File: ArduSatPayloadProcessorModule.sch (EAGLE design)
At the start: 315 parts, among them IC1 ATMEGA328P QFN32, IC10 ATMEGA328P QFN32, IC11 ATMEGA328P QFN32, IC12 ATMEGA328P QFN32, IC13 ATMEGA328P QFN32, IC14 ATMEGA328P QFN32, IC15 ATMEGA328P QFN32, IC16 ATMEGA328P QFN32, IC17 TXB0104, IC18 TMP102, IC19 TMP102, IC2 ATMEGA328P QFN32, IC20 ATMEGA2561-16MU, IC21 MAX4372F, IC22 MAX4372F, IC23 MUX-74HC4067-QFNSMT, IC24 MUX-74HC4067-QFNSMT, IC3 ATMEGA328P QFN32, IC4 ATMEGA328P QFN32, IC5 ATMEGA328P QFN32, IC6 ATMEGA328P QFN32, IC7 ATMEGA328P QFN32, IC8 ATMEGA328P QFN32, IC9 ATMEGA328P QFN32, P1 microSD, Q1 RJU003N03 N-MOSFET, Q10 RJU003N03 N-MOSFET, Q11 RJU003N03 N-MOSFET, Q12 RJU003N03 N-MOSFET, Q13 RJU003N03 N-MOSFET, Q14 RJU003N03 N-MOSFET, Q15 RJU003N03 N-MOSFET, Q16 RJU003N03 N-MOSFET, Q17 RJU003N03 N-MOSFET, Q18 RJU003N03 N-MOSFET, Q19 RJU003N03 N-MOSFET, Q2 RJU003N03 N-MOSFET, Q20 RJU003N03 N-MOSFET, Q21 RJU003N03 N-MOSFET, Q22 RJU003N03 N-MOSFET, Q23 RJU003N03 N-MOSFET, Q24 RJU003N03 N-MOSFET, Q25 RJU003N03 N-MOSFET, Q26 RJU003N03 N-MOSFET, Q27 RJU003N03 N-MOSFET, Q28 RJU003N03 N-MOSFET, Q29 RJU003N03 N-MOSFET, Q3 RJU003N03 N-MOSFET, Q30 RJU003N03 N-MOSFET, Q31 RJU003N03 N-MOSFET, Q32 RJU003N03 N-MOSFET, Q33 RJU003N03 N-MOSFET, Q34 RJU003N03 N-MOSFET, Q35 RJU003N03 N-MOSFET, Q36 RJU003N03 N-MOSFET, Q39 RJU003N03 N-MOSFET, Q4 RJU003N03 N-MOSFET, Q40 RJU003N03 N-MOSFET, Q41 RJU003N03 N-MOSFET, Q42 RJU003N03 N-MOSFET, Q43 RJU003N03 N-MOSFET, Q44 RJU003N03 N-MOSFET, Q45 RJU003N03 N-MOSFET, Q46 RJU003N03 N-MOSFET, Q5 RJU003N03 N-MOSFET, Q6 RJU003N03 N-MOSFET, Q7 RJU003N03 N-MOSFET, Q8 RJU003N03 N-MOSFET, Q9 RJU003N03 N-MOSFET, SW1 ADG801 SOT23-6, SW10 ADG801 SOT23-6, SW11 ADG801 SOT23-6, SW12 ADG801 SOT23-6, SW13 ADG801 SOT23-6, SW14 ADG801 SOT23-6, SW15 ADG801 SOT23-6, SW16 ADG801 SOT23-6, SW17 RESET, SW2 ADG801 SOT23-6, SW3 ADG801 SOT23-6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

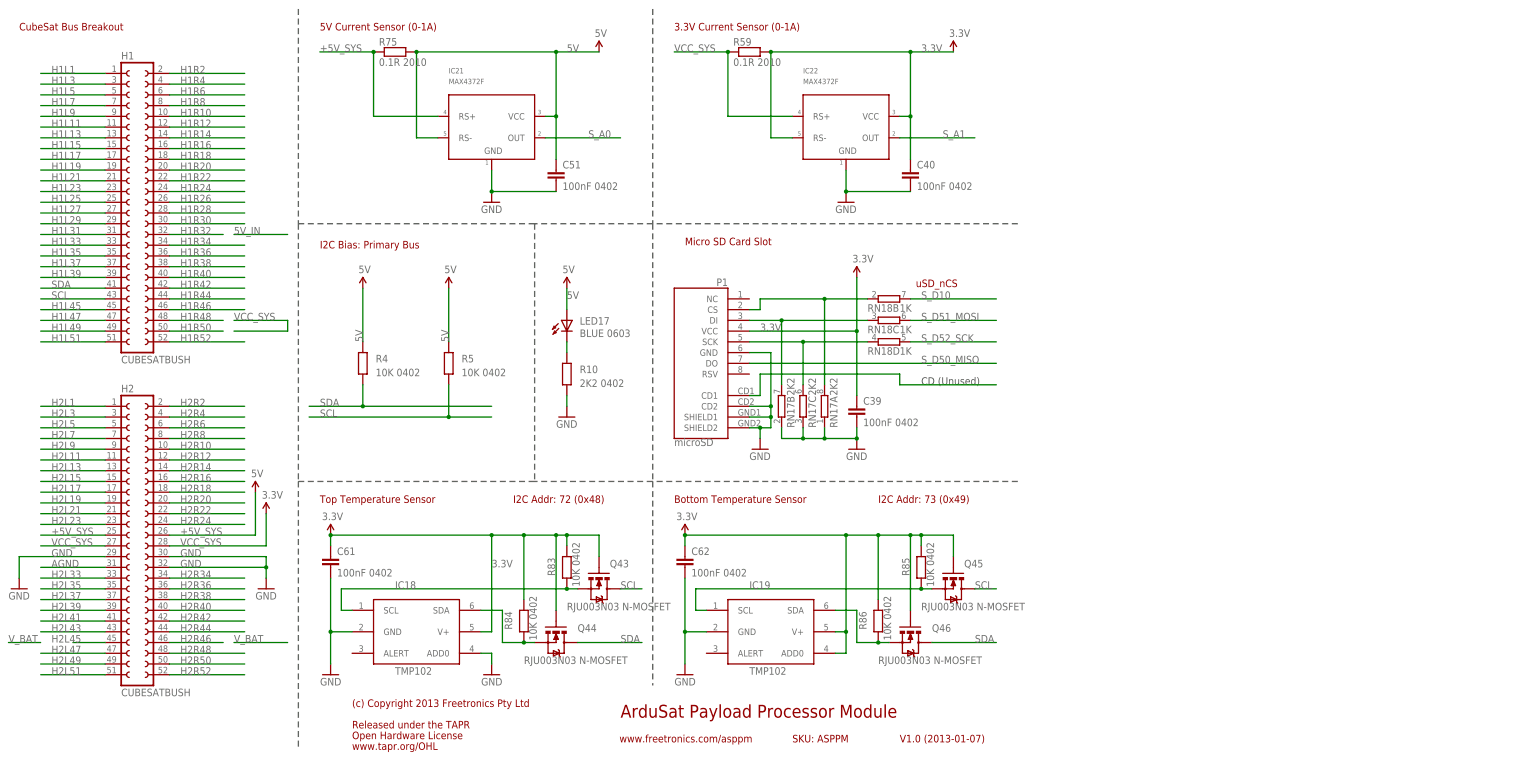
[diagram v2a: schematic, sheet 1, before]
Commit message: Fixed ISP pin assignment Added D13 LED to supervisor Fixed TX/RX from supervisor to multiplexers Replaced 4-pin debug connector with 6-pin connector in FTDI-type format Linked supervisor reset to debug connector GPS power now controlled by supervisor Input power from debug connector now goes through 5V current sensor Switched Cubesat Bus power links to H1-51 (5V) and H1-52 (3.3V) Added cut-track jumpers to select power link source Linked debug console to Cubesat Bus H1-34 (TXO) and H1-36 (RXD) Moved debug connector away from edge to increase solar panel clearance
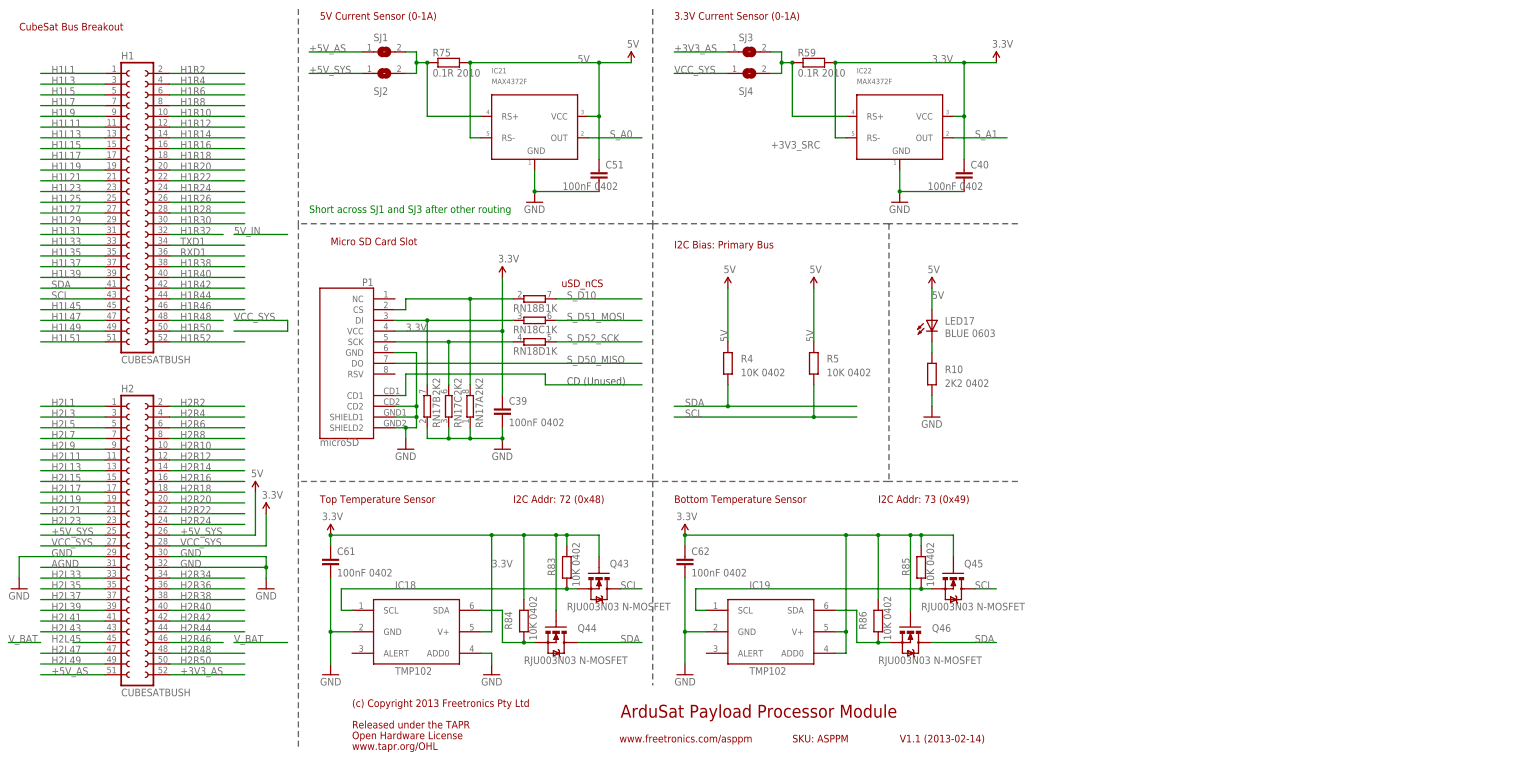
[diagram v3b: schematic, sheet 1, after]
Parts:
- added C58: 100nF 0402, freetronics-jon:C-EU0402C
- added LED18: BLUE 0603, freetronics-jon:LED0402
- added R81: 2K2 0402, freetronics-jon:RESISTOR0402
- added SJ1, SJ2, SJ3, SJ4: (no value), freetronics-master-v1.1:SJ
- added SW18: ADG801 SOT23-6, freetronics-jon:ADG801SOT23-6
- C13, C14: value 22pF 0603 -> 22pF 0402
- JP1: device pinhead:PINHD-1X4/90 -> freetronics-master-v1:M06RA
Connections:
- removed net AREF: C14.2, IC20.XTAL1, R32.1, XTL17.XTL2
- removed net H1R34: H1.34
- removed net H1R36: H1.36
- removed net H2L51: H2.51
- removed net H2R52: H2.52
- new net +3V3_AS: H2.52, SJ3.1
- new net +3V3_SRC: IC22.RS+, R59.1, SJ3.2, SJ4.2
- new net +5V_AS: H2.51, SJ1.1
- new net +5V_SRC: IC21.RS+, JP1.3, R75.1, SJ1.2, SJ2.2
- new net GPS_5V: C60.+, SW18.D, X2-1.S
- new net N$9998: LED18.C, R81.2
- new net PWR_GPS: IC20.(T1)PD6, SW18.IN
- new net RTS: C58.1, JP1.6
- new net XTAL2: C13.2, IC20.XTAL2, R32.2, XTL17.XTL1
- net +5V_SYS: now also SJ2.1; no longer IC21.RS+, R75.1
- net 5V: now also SW18.S, SW18.VDD; no longer C60.+, JP1.2, X2-1.S
- net D0_RX: now also H19.4, IC23.Z; no longer IC24.Z
- net D1_TX: now also H19.1, IC24.Z; no longer IC23.Z
- net GND: now also JP1.2, R81.1, SW18.GND
- net RXD1: now also H1.36, JP1.4; no longer JP1.3
- net S_D13: now also LED18.A
- net S_D50_MISO: no longer H19.1
- net S_D51_MOSI: no longer H19.4
- net S_RESET: now also C58.2
- net TXD1: now also H1.34, JP1.5; no longer JP1.4
- net VCC_SYS: now also SJ4.1; no longer IC22.RS+, R59.1
- net XTAL1: now also C14.2, IC20.XTAL1, R32.1, XTL17.XTL2; no longer C13.2, IC20.XTAL2, R32.2, XTL17.XTL1
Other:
- note added: "GPS Power Control"
- note added: "Short across SJ1 and SJ3 after other routing"
- note added: "TODO: DONE: Add D13 LED to supervisor Fix TX/RX to multiplexors Fix supervisor PDI / PDO Make debug console match FTDI standard Control GPS power from supervisor Monitor current when powered via console port Power from different bus pins. SJs to existing pins. Route 5V from H1-51 instead of H2-25/26 Route 3.3V from H1-52 instead of H2-27/28 Lay out debug USART1 to stack header on positions H1-34 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"
- note added: "V1.1 (2013-02-14)"
- note removed: "Debug was connected to VCC_SYS, I switched it to 5V. Is that OK?"
- note removed: "V1.0 (2013-01-07)"
- moved on the sheet: C39, C40, C51, IC21, IC22, LED17, P1, R10, R4, R5, R59, R75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

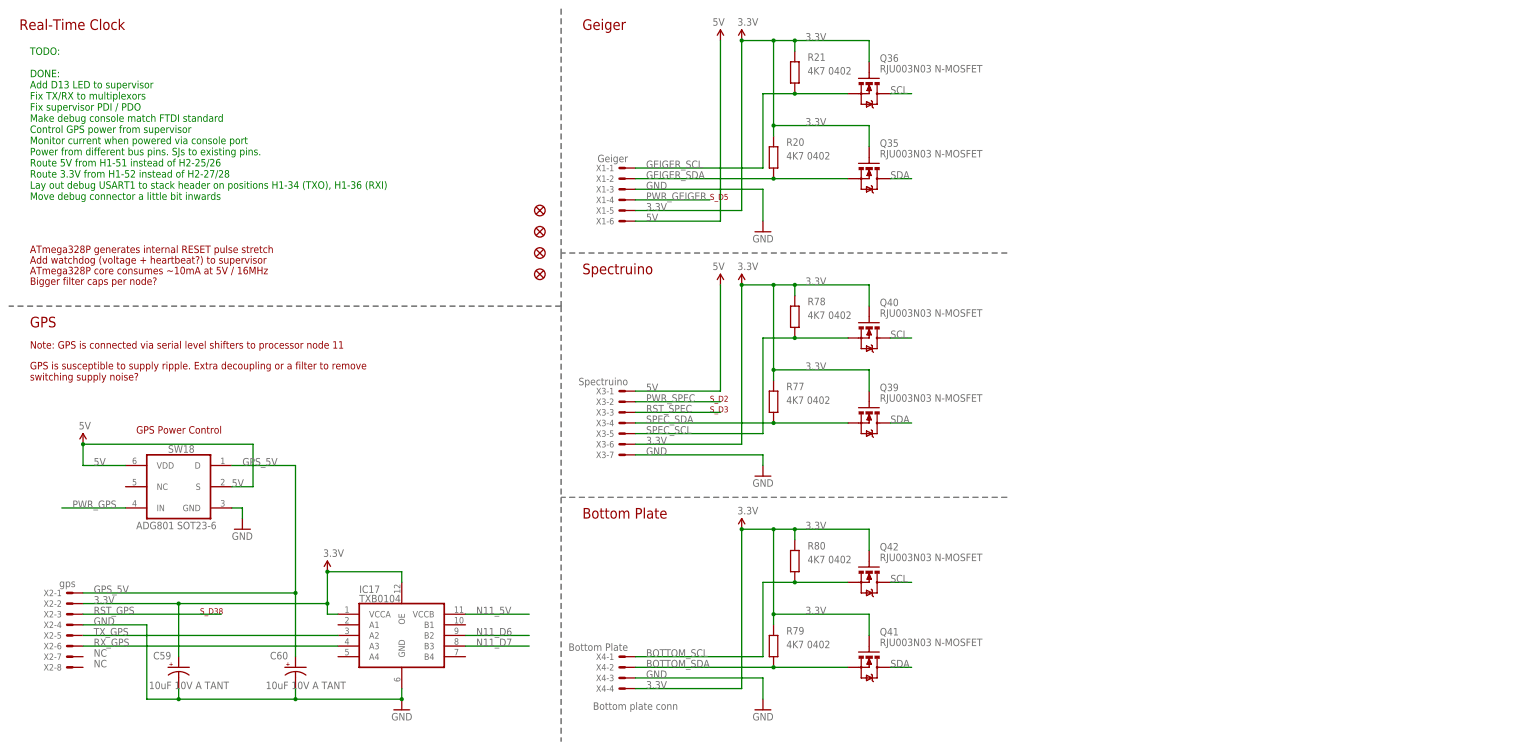
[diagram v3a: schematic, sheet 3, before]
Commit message: Added labels for power source selection jumpers; added parts for node reset latch
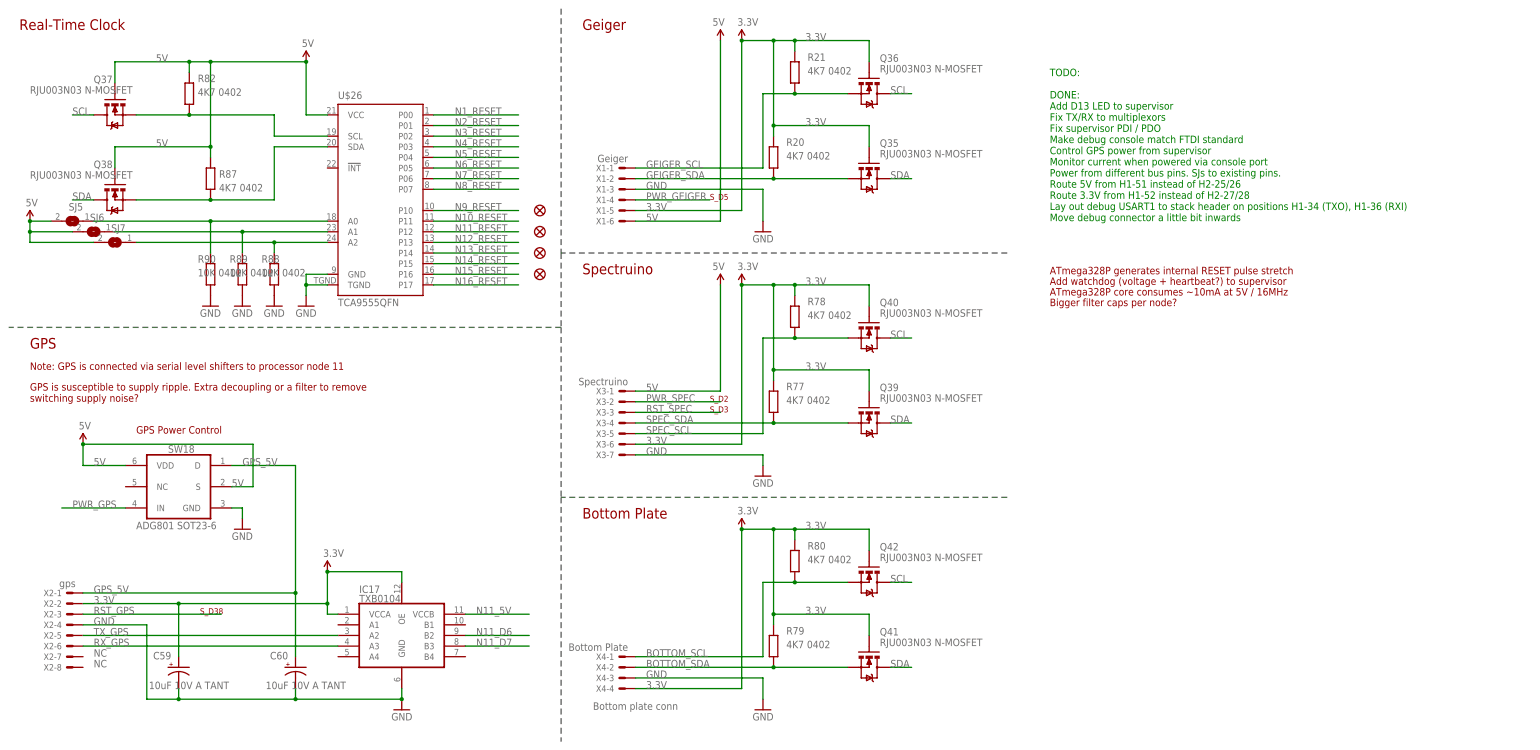
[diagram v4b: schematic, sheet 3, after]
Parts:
- added Q37, Q38: RJU003N03 N-MOSFET, freetronics-jon:MOSFET-NSOT-323
- added R82, R87: 4K7 0402, freetronics-jon:RESISTOR0402
- added R88, R89, R90: 10K 0402, freetronics-jon:RESISTOR0402
- added SJ5, SJ6, SJ7: (no value), freetronics-master-v1:SJ
- added U$26: TCA9555QFN, freetronics-jon:TCA9555QFN
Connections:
- removed net H1L51: H1.51
- removed net H1R52: H1.52
- new net H2L51: H2.51
- new net H2R52: H2.52
- new net N$10000: R90.2, SJ5.1, U$26.A0
- new net N$10004: R89.2, SJ6.1, U$26.A1
- new net N$10005: R88.2, SJ7.1, U$26.A2
- new net N$10006: Q37.S, R82.1, U$26.SCL
- new net N$10007: Q38.S, R87.1, U$26.SDA
- net +3V3_AS: now also H1.52; no longer H2.52
- net +5V_AS: now also H1.51; no longer H2.51
- net 5V: now also Q37.G, Q38.G, R82.2, R87.2, SJ5.2, SJ6.2, SJ7.2, U$26.VCC
- net GND: now also R88.1, R89.1, R90.1, U$26.GND, U$26.TGND
- net N10_RESET: now also U$26.P11
- net N11_RESET: now also U$26.P12
- net N12_RESET: now also U$26.P13
- net N13_RESET: now also U$26.P14
- net N14_RESET: now also U$26.P15
- net N15_RESET: now also U$26.P16
- net N16_RESET: now also U$26.P17
- net N1_RESET: now also U$26.P00
- net N2_RESET: now also U$26.P01
- net N3_RESET: now also U$26.P02
- net N4_RESET: now also U$26.P03
- net N5_RESET: now also U$26.P04
- net N6_RESET: now also U$26.P05
- net N7_RESET: now also U$26.P06
- net N8_RESET: now also U$26.P07
- net N9_RESET: now also U$26.P10
- net SCL: now also Q37.D
- net SDA: now also Q38.D

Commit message: Start of placement and fan-out of node reset latch
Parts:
- SJ5, SJ6, SJ7: device freetronics-master-v1:SJ -> freetronics-jon:SJ0402O
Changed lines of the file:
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@@
 <part name="GND110" library="freetronics" deviceset="GND" device=""/>
 <part name="GND111" library="freetronics" deviceset="GND" device=""/>
-<part name="SJ5" library="freetronics-master-v1" deviceset="SJ" device=""/>
-<part name="SJ6" library="freetronics-master-v1" deviceset="SJ" device=""/>
-<part name="SJ7" library="freetronics-master-v1" deviceset="SJ" device=""/>
+<part name="SJ5" library="freetronics-jon" deviceset="SJ" device="0402O"/>
+<part name="SJ6" library="freetronics-jon" deviceset="SJ" device="0402O"/>
+<part name="SJ7" library="freetronics-jon" deviceset="SJ" device="0402O"/>
 <part name="U$24" library="SparkFun" deviceset="5V" device=""/>
 <part name="U$26" library="freetronics-jon" deviceset="TCA9555" device="QFN"/>

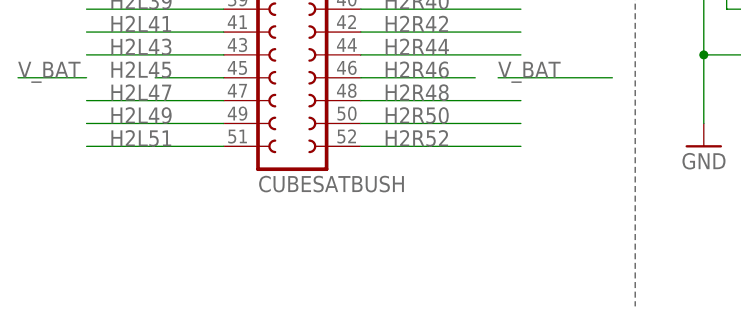
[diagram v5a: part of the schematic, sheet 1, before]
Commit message: Clearance and label improvements
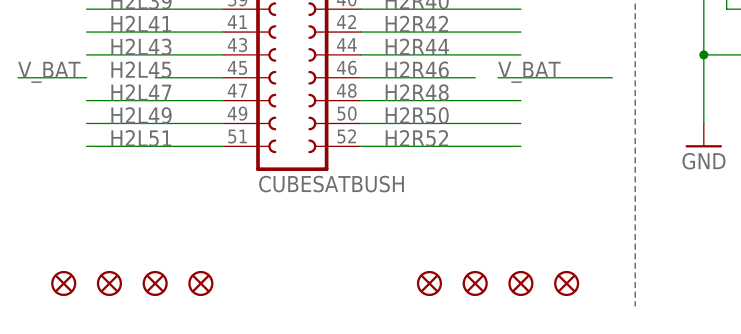
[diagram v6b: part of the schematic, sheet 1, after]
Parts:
- added FID5, FID6, FID7, FID8: FIDUCIAL1X2.5, freetronics:FIDUCIAL1X2.5
- SJ7: value (none) -> SJC0402; device freetronics-jon:SJ0402O -> freetronics-jon:SJC0402
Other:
- note added: "Node Reset Control"
- note removed: "Real-Time Clock"
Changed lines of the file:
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@@
 <part name="SJ5" library="freetronics-jon" deviceset="SJ" device="0402O"/>
 <part name="SJ6" library="freetronics-jon" deviceset="SJ" device="0402O"/>
-<part name="SJ7" library="freetronics-jon" deviceset="SJ" device="0402O"/>
+<part name="SJ7" library="freetronics-jon" deviceset="SJC" device="0402"/>
 <part name="U$24" library="SparkFun" deviceset="5V" device=""/>
 <part name="U$26" library="freetronics-jon" deviceset="TCA9555" device="QFN"/>
+<part name="FID5" library="freetronics" deviceset="FIDUCIAL" device="1X2.5"/>
+<part name="FID6" library="freetronics" deviceset="FIDUCIAL" device="1X2.5"/>
+<part name="FID7" library="freetronics" deviceset="FIDUCIAL" device="1X2.5"/>
+<part name="FID8" library="freetronics" deviceset="FIDUCIAL" device="1X2.5"/>
 </parts>
 <sheets>
@@
 <instance part="GND70" gate="1" x="121.92" y="76.2"/>
 <instance part="P+6" gate="G$1" x="121.92" y="116.84"/>
+<instance part="FID1" gate="G$1" x="20.32" y="7.62" rot="R90"/>
+<instance part="FID2" gate="G$1" x="25.4" y="7.62" rot="R90"/>
+<instance part="FID3" gate="G$1" x="15.24" y="7.62" rot="R90"/>
+<instance part="FID4" gate="G$1" x="10.16" y="7.62" rot="R90"/>
+<instance part="FID5" gate="G$1" x="60.96" y="7.62" rot="R90"/>
+<instance part="FID6" gate="G$1" x="66.04" y="7.62" rot="R90"/>
+<instance part="FID7" gate="G$1" x="55.88" y="7.62" rot="R90"/>
+<instance part="FID8" gate="G$1" x="50.8" y="7.62" rot="R90"/>
 </instances>
 <busses>
@@
 <plain>
 <frame x1="0" y1="0" x2="248.92" y2="185.42" columns="8" rows="5" layer="94"/>
-<text x="7.62" y="175.26" size="2.54" layer="94" ratio="12">Real-Time Clock</text>
+<text x="7.62" y="175.26" size="2.54" layer="94" ratio="12">Node Reset Control</text>
 <text x="144.78" y="70.612" size="1.778" layer="103">Spectruino conn</text>
 <text x="12.954" y="19.812" size="1.778" layer="103">GPS conn</text>
@@
 </instance>
 <instance part="P+7" gate="G$1" x="81.28" y="45.72"/>
-<instance part="FID1" gate="G$1" x="132.08" y="121.92"/>
-<instance part="FID2" gate="G$1" x="132.08" y="116.84"/>
-<instance part="FID3" gate="G$1" x="132.08" y="127"/>
-<instance part="FID4" gate="G$1" x="132.08" y="132.08"/>
 <instance part="GND107" gate="1" x="60.96" y="55.88"/>
 <instance part="SW18" gate="G$1" x="45.72" y="66.04" smashed="yes">
@@
 <instance part="SJ5" gate="1" x="20.32" y="129.54" rot="MR0"/>
 <instance part="SJ6" gate="1" x="25.4" y="127" rot="MR0"/>
-<instance part="SJ7" gate="1" x="30.48" y="124.46" rot="MR0"/>
+<instance part="SJ7" gate="G$1" x="30.48" y="124.46" rot="MR0"/>
 <instance part="U$24" gate="G$1" x="10.16" y="129.54"/>
 <instance part="U$26" gate="G$1" x="93.98" y="134.62"/>
@@
 <wire x1="20.32" y1="127" x2="10.16" y2="127" width="0.1524" layer="91"/>
 <wire x1="10.16" y1="127" x2="10.16" y2="129.54" width="0.1524" layer="91"/>
-<pinref part="SJ7" gate="1" pin="2"/>
+<pinref part="SJ7" gate="G$1" pin="2"/>
 <wire x1="25.4" y1="124.46" x2="10.16" y2="124.46" width="0.1524" layer="91"/>
 <wire x1="10.16" y1="124.46" x2="10.16" y2="127" width="0.1524" layer="91"/>
@@
 <wire x1="68.58" y1="121.92" x2="68.58" y2="124.46" width="0.1524" layer="91"/>
 <junction x="68.58" y="124.46"/>
-<pinref part="SJ7" gate="1" pin="1"/>
+<pinref part="SJ7" gate="G$1" pin="1"/>
 <pinref part="U$26" gate="G$1" pin="A2"/>
 </segment>

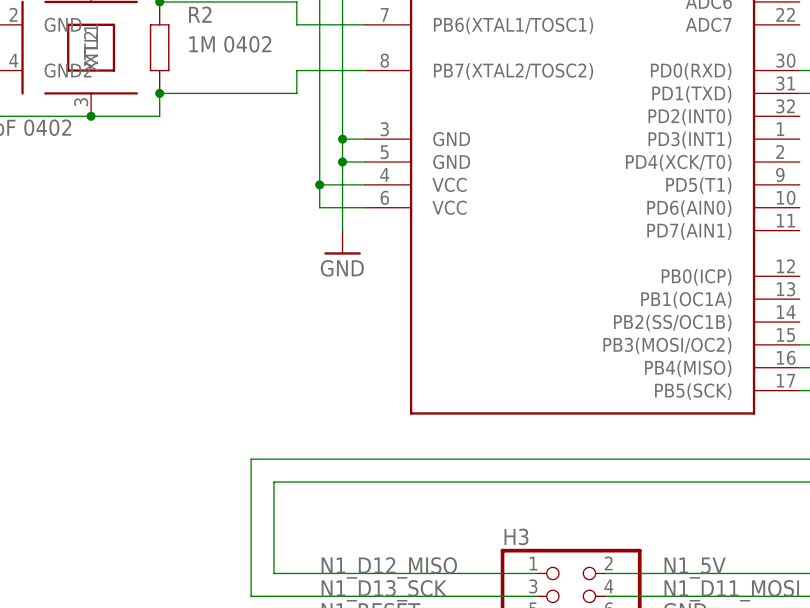
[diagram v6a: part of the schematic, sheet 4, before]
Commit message: Re-routed around MCU GND pads and improved footprints
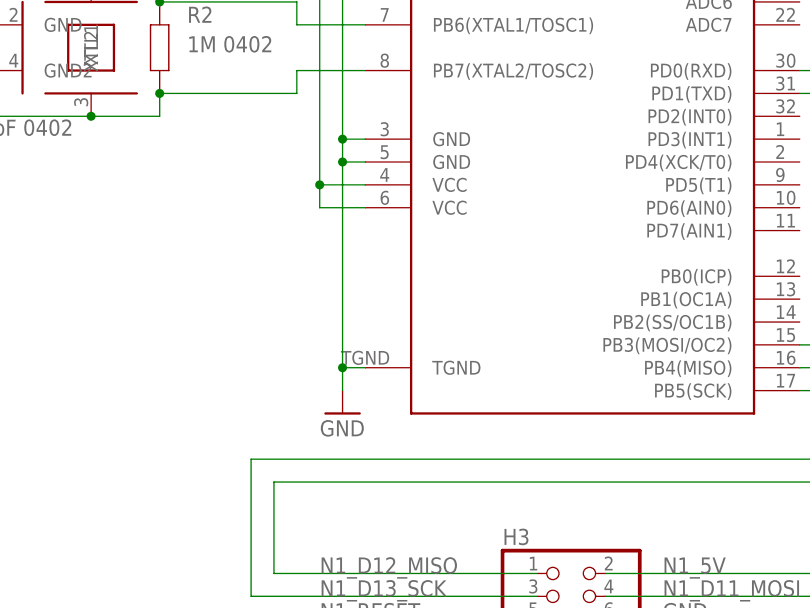
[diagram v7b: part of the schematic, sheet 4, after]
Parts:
- IC1, IC10, IC11, IC12, IC13, IC14, IC15, IC16, IC2, IC3, IC4, IC5, IC6, IC7, IC8, IC9: device freetronics-master-v1.1:AVR-MEGA8-MI -> freetronics-jon:AVR-MEGA8-MI
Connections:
- net GND: now also IC1.TGND, IC10.TGND, IC11.TGND, IC12.TGND, IC13.TGND, IC14.TGND, IC15.TGND, IC16.TGND, IC2.TGND, IC3.TGND, IC4.TGND, IC5.TGND, IC6.TGND, IC7.TGND, IC8.TGND, IC9.TGND
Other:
- note added: "Short across SJ1 after other routing"
- note added: "Short across SJ3 after other routing"
- note removed: "Short across SJ1 and SJ3 after other routing"
- note removed: "TODO: DONE: Add D13 LED to supervisor Fix TX/RX to multiplexors Fix supervisor PDI / PDO Make debug console match FTDI standard Control GPS power from supervisor Monitor current when powered via console port Power from different bus pins. SJs to existing pins. Route 5V from H1-51 instead of H2-25/26 Route 3.3V from H1-52 instead of H2-27/28 Lay out debug USART1 to stack header on positions H1-34 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"
